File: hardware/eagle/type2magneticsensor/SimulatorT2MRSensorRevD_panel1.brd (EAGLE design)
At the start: 48.3 x 48.3 mm, 10 parts

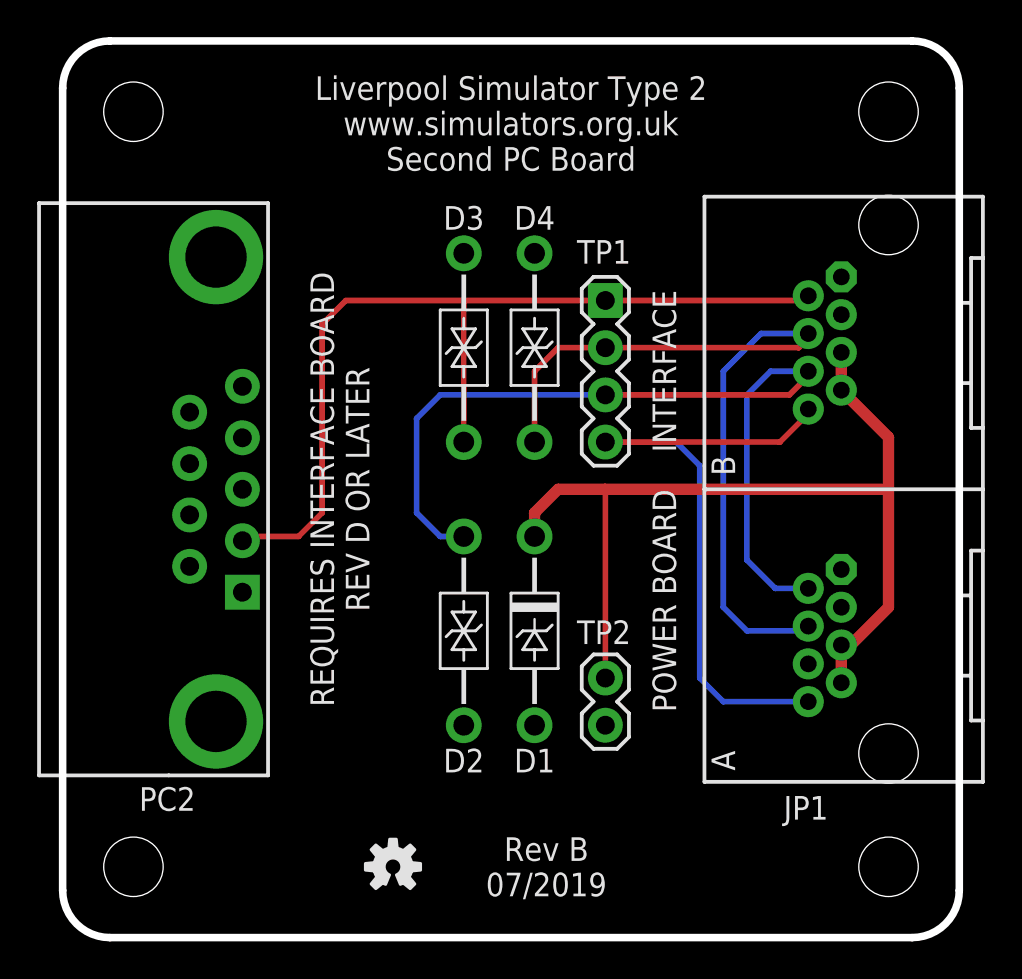
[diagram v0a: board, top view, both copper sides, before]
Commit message: Board Housekeeping
URL on silkscreens, caution messages, tidy up naming conventions.
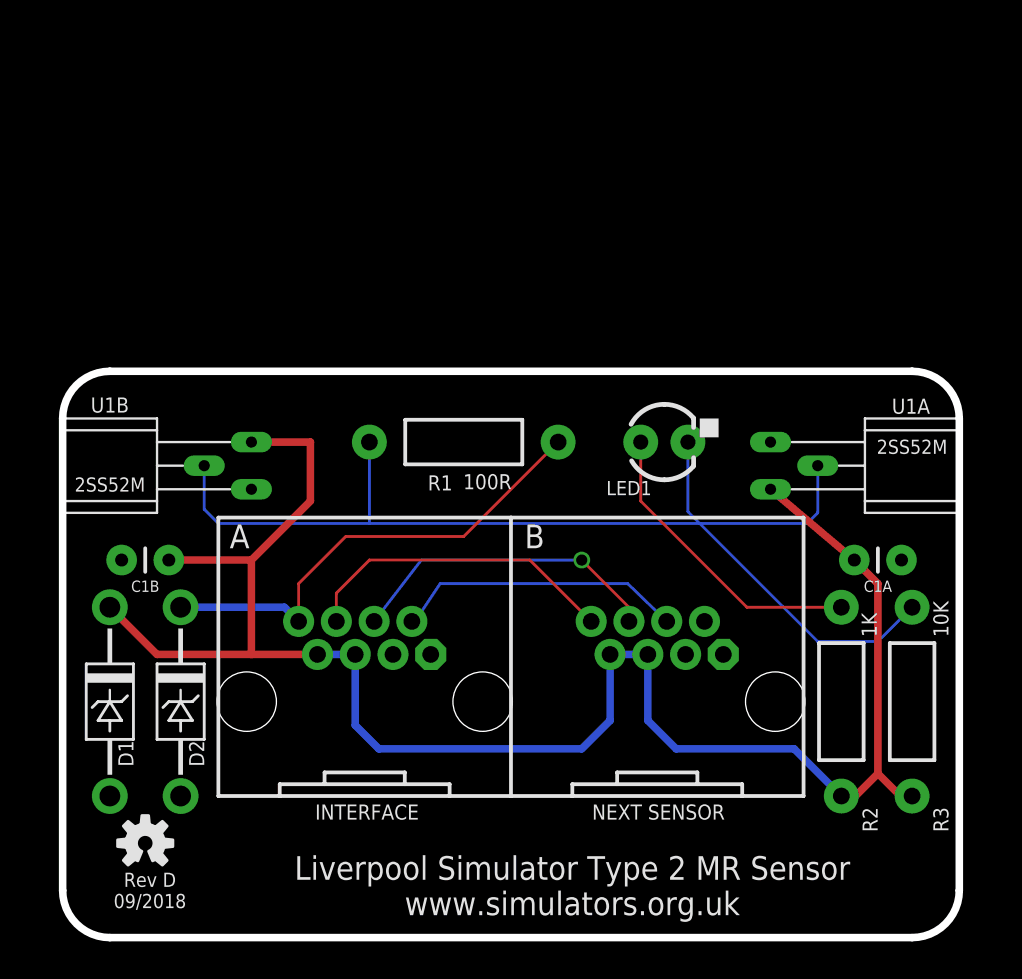
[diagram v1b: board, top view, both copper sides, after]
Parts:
- removed D3, D4: SA15CA, AIC_Custom:DO41_TVS_BI
- removed PC2: (no value), AIC_Custom:MULTICOMP-DB9-FEMALE-PCB-90DEG
- removed TP1: (no value), SparkFun-Connectors:1X04
- removed TP2: (no value), SparkFun-Connectors:1X02
- removed U$1: (no value), AIC_Custom:WARNING_TRIANGLE_TPLACE
- added C1A, C1B: 100nF, SparkFun-Passives:CAP-PTH-SMALL
- added E$1: (no value), AIC_Custom:WARNING_TRIANGLE_TPLACE
- added LED1: Blue, SparkFun-LED:LED3MM
- added R1: 100R, SparkFun-Passives:AXIAL-0.4
- added R2: 1K, SparkFun-Passives:AXIAL-0.4
- added R3: 10K, SparkFun-Passives:AXIAL-0.4
- added U1A, U1B: 2SS52MOFFSET, AIC_Custom:2SS52M_FLAT_OFFSET
- D1: value SA12A -> SA5.0A
- D2: value SA15CA -> SA5.0A; device AIC_Custom:DO41_TVS_BI -> AIC_Custom:DO41_TVS_UNI
- JP1: value RJ45-RJHSE-5080-022HOLE -> RJ45-RJHSE-5080-023HOLE; device AIC_Custom:RJ45-RJHSE-5080-02 -> AIC_Custom:RJ45-RJHSE-5080-02-3HOLE
- moved JP1 23.3 mm to (24.1, 12.7), turned to 0 degrees
- moved D1 23.2 mm to (2.54, 12.7)
- moved D2 15.7 mm to (6.35, 12.7), turned to 90 degrees
- moved LOGO1 13.4 mm to (4.45, 5.08)
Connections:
- removed net P8: JP1.A8, JP1.B8, TP1.4
- removed net RXD: D4.C, JP1.A4, JP1.B4, TP1.2
- removed net TX2: D2.C, JP1.A2, JP1.B6, TP1.3
- removed net TXD: D3.C, JP1.B2, PC2.2, TP1.1
- removed net VIN2: D1.CATHODE, JP1.A5, JP1.A7, JP1.B5, JP1.B7, TP2.1
- new net !OUT!: D2.CATHODE, JP1.A8, R1.P$1
- new net B2: JP1.A6, JP1.B8
- new net B3: JP1.A4, JP1.B6
- new net B4: JP1.A2, JP1.B4
- new net LED: LED1.A, R2.P$1
- new net SIG: LED1.K, R1.P$2, R3.P$1, U1A.P$2, U1B.P$2
- new net VCC: C1A.1, C1B.1, D1.CATHODE, JP1.A5, JP1.A7, JP1.B5, JP1.B7, R2.P$2, R3.P$2, U1A.P$3, U1B.P$3
- net GND: now also C1A.2, C1B.2, D2.ANODE, U1A.P$1, U1B.P$1; no longer D2.A, D3.A, D4.A, PC2.5, TP2.2
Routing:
- net VCC: track 0.00 -> 97.3 mm
- net SIG: track 0.00 -> 62.3 mm
- net VIN2: track 51.2 -> 0.00 mm
- net TXD: track 49.5 -> 0.00 mm
- net TX2: track 47.1 -> 0.00 mm
- net RXD: track 42.8 -> 0.00 mm
- net P8: track 35.2 -> 0.00 mm
- net !OUT!: track 0.00 -> 26.0 mm
- net B2: track 0.00 -> 17.3 mm
- net B3: track 0.00 -> 17.2 mm, vias 0 -> 1
- net LED: track 0.00 -> 16.3 mm
- net B4: track 0.00 -> 15.6 mm
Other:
- board size 48.3 x 48.3 mm -> 48.3 x 30.5 mm
- board text added: "2SS52M Lead Forming Guide"
- board text added: "C1A"
- board text added: "C1B"
- board text added: "D1"
- board text added: "D2"
- board text added: "INTERFACE"
- board text added: "LED1"
- board text added: "Liverpool Simulator Type 2 MR Sensor www.simulators.org.uk"
- board text added: "NEXT SENSOR"
- board text added: "R1"
- board text added: "R2"
- board text added: "R3"
- board text added: "Rev D 09/2018"
- board text added: "U1A"
- board text added: "U1B"
- board text removed: "Liverpool Simulator Type 2 www.simulators.org.uk Second PC Board"
- board text removed: "POWER BOARD INTERFACE"
- board text removed: "REQUIRES INTERFACE BOARD REV D OR LATER"
- board text removed: "Rev B 07/2019"
